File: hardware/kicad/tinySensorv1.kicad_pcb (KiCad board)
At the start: 2 copper layers, 94 x 60 mm, 32 parts, among them J1 RADIO, J10 CR2032 socket, J11 AAA socket, J12 AA Socket, J13 RAW IN, J2 DCDC converter, J3 BMP/BME breakout, J4 PWM out, J5 OneWire sensor, J6 ISP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

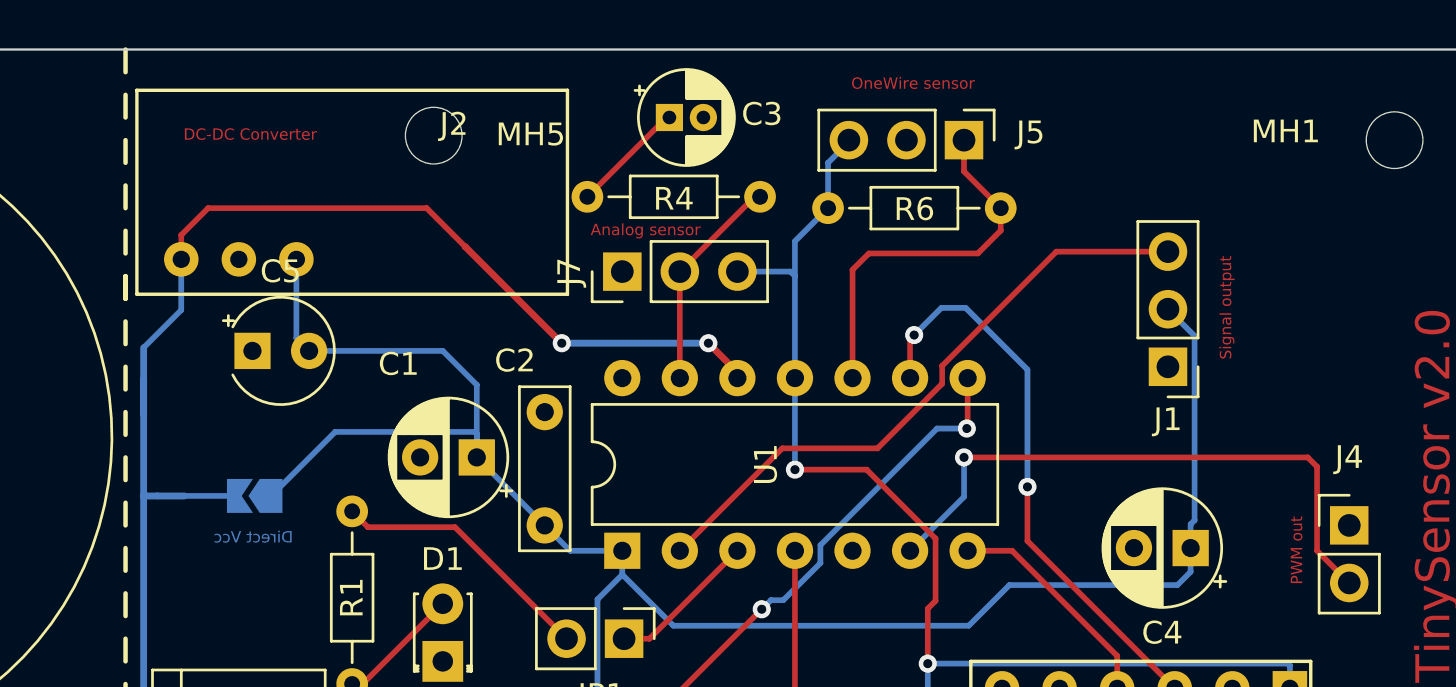
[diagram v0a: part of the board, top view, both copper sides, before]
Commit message: feat: Last enhancements from hardware testing
* Full LM35 support: <0 temp with diode support
* 433Mhz emitter is powered by SENSOR_VCC
* Enhanced layout
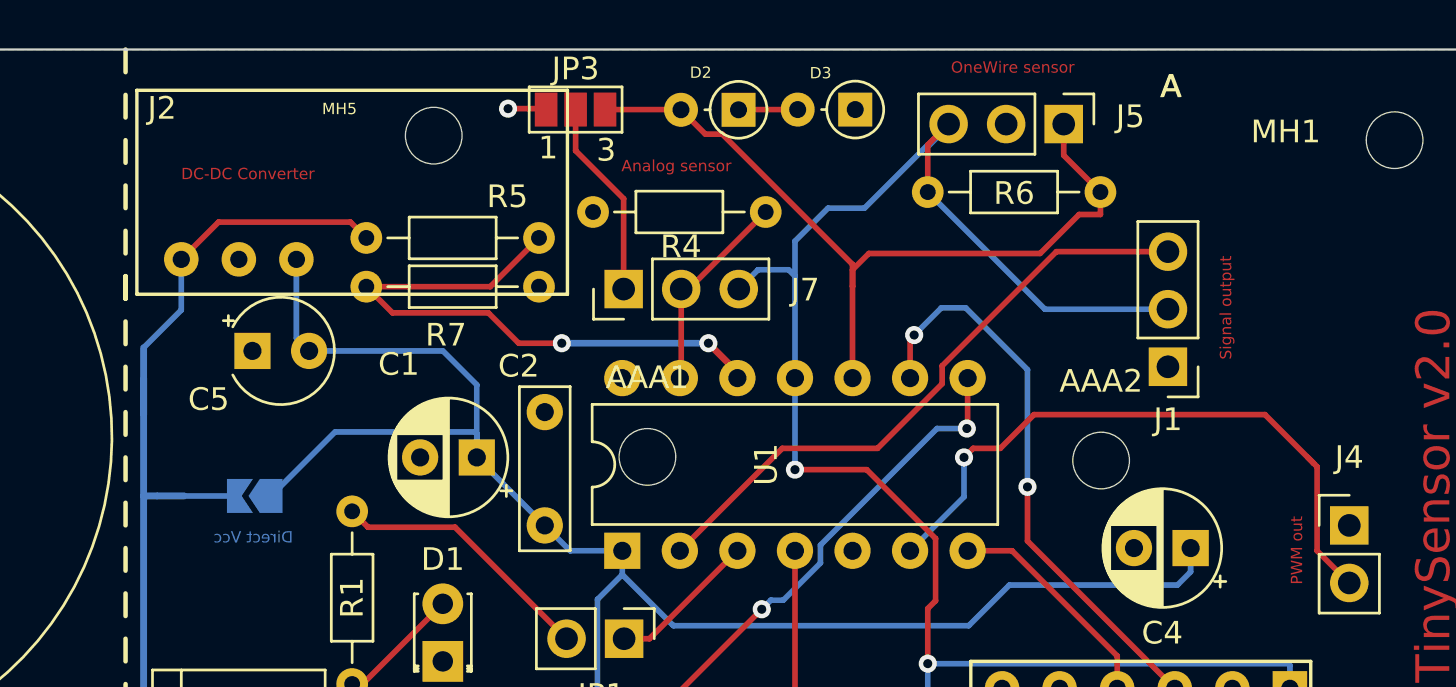
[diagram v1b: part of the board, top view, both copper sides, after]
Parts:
- removed C3: 1u, Capacitor_THT:CP_Radial_D4.0mm_P1.50mm
- added AAA1: MountingHole, MountingHole:MountingHole_2.5mm, F.Cu at (170.0, 66.0)
- added AAA2: MountingHole, MountingHole:MountingHole_2.5mm, F.Cu at (190.1, 66.1)
- added D2: 1N4001, Diode_THT:D_DO-34_SOD68_P2.54mm_Vertical_AnodeUp, F.Cu at (174.1, 50.7)
- added D3: 1N4001, Diode_THT:D_DO-34_SOD68_P2.54mm_Vertical_AnodeUp, F.Cu at (179.2, 50.6)
- added JP3: Ground ref, Jumper:SolderJumper-3_P1.3mm_Open_Pad1.0x1.5mm_NumberLabels, F.Cu at (166.9, 50.6)
- added R5: 1k, Resistor_THT:R_Axial_DIN0204_L3.6mm_D1.6mm_P7.62mm_Horizontal, F.Cu at (165.2, 56.3)
- added R7: 1k, Resistor_THT:R_Axial_DIN0204_L3.6mm_D1.6mm_P7.62mm_Horizontal, F.Cu at (165.2, 58.5)
- R4: value 75R -> 18k
- moved J5 4.46 mm to (188.4, 51.3)
- moved R6 4.46 mm to (182.4, 54.3)
- moved J7 0.77 mm to (169.0, 58.6)
- moved R4 0.72 mm to (175.2, 55.2)
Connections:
- net /OneWire renamed /OneWire_and_analog_bias
- J1 pad 2: VCC -> /SENSOR_VCC
- J7 pad 1: GND -> Net-(J7-Pad1)
- R4 pad 2: Net-(C3-Pad1) -> GND
- U1 pad 12: +BATT -> /Battery_Checker
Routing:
- net /Battery_Checker: track 0.00 -> 26.7 mm, vias 0 -> 2
- net /SENSOR_VCC: track 53.0 -> 74.3 mm
- net +BATT: track 127.8 -> 107.6 mm, vias 2 -> 0
- net /OneWire_and_analog_bias: track 16.7 -> 36.1 mm
- net VCC: track 85.0 -> 73.9 mm
- net Net-(J7-Pad1): track 0.00 -> 8.80 mm
- net Net-(C3-Pad1): track 5.07 -> 0.00 mm
- net Net-(D2-Pad1): track 0.00 -> 2.61 mm
- net /PWM_OUT: track 26.6 -> 28.5 mm
- net GND: track 0.03 -> 1.72 mm, vias 0 -> 1
- net /Analog_sensor: track 9.61 -> 9.09 mm

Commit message: layout enhancements
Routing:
- net /TX_RADIO: track 27.5 -> 29.8 mm
- net /OneWire_and_analog_bias: track 36.1 -> 37.7 mm
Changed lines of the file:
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@@
     (thickness 1.6)
     (drawings 94)
-    (tracks 179)
+    (tracks 180)
     (zones 0)
     (modules 38)
@@
     (solder_mask_min_width 0.25)
     (aux_axis_origin 0 0)
+    (grid_origin 172.92 51.7)
     (visible_elements 7FFDFFFF)
     (pcbplotparams
@@
     (add_net VCC)
   )
+  (module Jumper:SolderJumper-3_P1.3mm_Open_Pad1.0x1.5mm_NumberLabels (layer F.Cu)
+    (at 166.86 50.65)
+    (descr "SMD Solder Jumper, 1x1.5mm Pads, 0.3mm gap, open, labeled with numbers")
+    (tags "solder jumper open")
+    (attr virtual)
+    (fp_text reference JP3 (at 0 -1.8) (layer F.SilkS)
+      (effects (font (size 1 1) (thickness 0.15)))
+    )
+    (fp_text value "Ground ref" (at 0 1.9) (layer F.Fab)
+      (effects (font (size 1 1) (thickness 0.15)))
+    )
+    (fp_line (start 2.3 1.25) (end -2.3 1.25) (layer F.CrtYd) (width 0.05))
+    (fp_line (start 2.3 1.25) (end 2.3 -1.25) (layer F.CrtYd) (width 0.05))
+    (fp_line (start -2.3 -1.25) (end -2.3 1.25) (layer F.CrtYd) (width 0.05))
+    (fp_line (start -2.3 -1.25) (end 2.3 -1.25) (layer F.CrtYd) (width 0.05))
+    (fp_line (start -2.05 -1) (end 2.05 -1) (layer F.SilkS) (width 0.12))
+    (fp_line (start 2.05 -1) (end 2.05 1) (layer F.SilkS) (width 0.12))
+    (fp_line (start 2.05 1) (end -2.05 1) (layer F.SilkS) (width 0.12))
+    (fp_line (start -2.05 1) (end -2.05 -1) (layer F.SilkS) (width 0.12))
+    (fp_text user 1 (at -2.6 0) (layer F.SilkS)
+      (effects (font (size 1 1) (thickness 0.15)))
+    )
+    (fp_text user 3 (at 2.6 0) (layer F.SilkS)
+      (effects (font (size 1 1) (thickness 0.15)))
+    )
+    (pad 1 smd rect (at -1.3 0) (size 1 1.5) (layers F.Cu F.Mask)
+      (net 6 GND))
+    (pad 2 smd rect (at 0 0) (size 1 1.5) (layers F.Cu F.Mask)
+      (net 18 "Net-(J7-Pad1)"))
+    (pad 3 smd rect (at 1.3 0) (size 1 1.5) (layers F.Cu F.Mask)
+      (net 20 /OneWire_and_analog_bias))
+  )
   (module MountingHole:MountingHole_2.5mm locked (layer F.Cu)
     (at 190.05 66.136918)
@@
       (effects (font (size 1 1) (thickness 0.15)))
     )
-    (fp_text user %R (at 1.27 -2.25566 180) (layer F.Fab)
+    (fp_text user %R (at 1.25 -1.92 180) (layer F.Fab)
       (effects (font (size 1 1) (thickness 0.15)))
     )
@@
       (rotate (xyz 0 0 0))
     )
-  )
-  (module Jumper:SolderJumper-3_P1.3mm_Open_Pad1.0x1.5mm_NumberLabels (layer F.Cu)
-    (at 166.86 50.65)
-    (descr "SMD Solder Jumper, 1x1.5mm Pads, 0.3mm gap, open, labeled with numbers")
-    (tags "solder jumper open")
-    (attr virtual)
-    (fp_text reference JP3 (at 0 -1.8) (layer F.SilkS)
-      (effects (font (size 1 1) (thickness 0.15)))
-    )
-    (fp_text value "Ground ref" (at 0 1.9) (layer F.Fab)
-      (effects (font (size 1 1) (thickness 0.15)))
-    )
-    (fp_text user 3 (at 1.35 1.79) (layer F.SilkS)
-      (effects (font (size 1 1) (thickness 0.15)))
-    )
-    (fp_text user 1 (at -1.21 1.69) (layer F.SilkS)
-      (effects (font (size 1 1) (thickness 0.15)))
-    )
-    (fp_line (start -2.05 1) (end -2.05 -1) (layer F.SilkS) (width 0.12))
-    (fp_line (start 2.05 1) (end -2.05 1) (layer F.SilkS) (width 0.12))
-    (fp_line (start 2.05 -1) (end 2.05 1) (layer F.SilkS) (width 0.12))
-    (fp_line (start -2.05 -1) (end 2.05 -1) (layer F.SilkS) (width 0.12))
-    (fp_line (start -2.3 -1.25) (end 2.3 -1.25) (layer F.CrtYd) (width 0.05))
-    (fp_line (start -2.3 -1.25) (end -2.3 1.25) (layer F.CrtYd) (width 0.05))
-    (fp_line (start 2.3 1.25) (end 2.3 -1.25) (layer F.CrtYd) (width 0.05))
-    (fp_line (start 2.3 1.25) (end -2.3 1.25) (layer F.CrtYd) (width 0.05))
-    (pad 3 smd rect (at 1.3 0) (size 1 1.5) (layers F.Cu F.Mask)
-      (net 20 /OneWire_and_analog_bias))
-    (pad 2 smd rect (at 0 0) (size 1 1.5) (layers F.Cu F.Mask)
-      (net 18 "Net-(J7-Pad1)"))
-    (pad 1 smd rect (at -1.3 0) (size 1 1.5) (layers F.Cu F.Mask)
-      (net 6 GND))
   )
   (module Resistor_THT:R_Axial_DIN0204_L3.6mm_D1.6mm_P7.62mm_Horizontal (layer F.Cu)
@@
     (effects (font (size 0.5 0.5) (thickness 0.125)) (justify mirror))
   )
-  (gr_text "OneWire sensor" (at 186.15 48.79) (layer F.Cu)
+  (gr_text "OneWire sensor" (at 185.77 49.2) (layer F.Cu)
     (effects (font (size 0.5 0.5) (thickness 0.125)))
   )
-  (gr_text "Analog sensor" (at 171.31 53.14) (layer F.Cu)
+  (gr_text "Analog sensor" (at 171.72 53.72) (layer F.Cu)
     (effects (font (size 0.5 0.5) (thickness 0.125)))
   )
@@
   (segment (start 170.12 74) (end 169 74) (width 0.25) (layer F.Cu) (net 2) (status 20))
   (segment (start 174 70.12) (end 170.12 74) (width 0.25) (layer F.Cu) (net 2) (status 10))
-  (segment (start 171.46 70.12) (end 175.98 65.6) (width 0.25) (layer F.Cu) (net 4) (status 10))
-  (segment (start 180.185002 65.6) (end 175.98 65.6) (width 0.25) (layer F.Cu) (net 4))
-  (segment (start 183.034999 62.750003) (end 180.185002 65.6) (width 0.25) (layer F.Cu) (net 4))
-  (segment (start 183.034999 61.959999) (end 183.034999 62.750003) (width 0.25) (layer F.Cu) (net 4))
-  (segment (start 188.074998 56.92) (end 183.034999 61.959999) (width 0.25) (layer F.Cu) (net 4))
-  (segment (start 193 56.92) (end 188.074998 56.92) (width 0.25) (layer F.Cu) (net 4) (status 10))
+  (segment (start 189.26 60.66) (end 193 56.92) (width 0.25) (layer F.Cu) (net 4))
+  (segment (start 182.96 60.66) (end 189.26 60.66) (width 0.25) (layer F.Cu) (net 4))
+  (segment (start 182.96 65.46) (end 182.96 60.66) (width 0.25) (layer F.Cu) (net 4))
+  (segment (start 182.82 65.6) (end 182.96 65.46) (width 0.25) (layer F.Cu) (net 4))
+  (segment (start 171.46 70.12) (end 175.98 65.6) (width 0.25) (layer F.Cu) (net 4))
+  (segment (start 175.98 65.6) (end 182.82 65.6) (width 0.25) (layer F.Cu) (net 4))
   (segment (start 190.76 76.66) (end 190.76 76.19) (width 0.25) (layer F.Cu) (net 5) (status 30))
   (segment (start 184.16 70.12) (end 186.12 70.12) (width 0.25) (layer F.Cu) (net 5) (status 10))
@@
   (segment (start 188.4 52.67) (end 190.02 54.29) (width 0.25) (layer F.Cu) (net 20) (status 20))
   (segment (start 188.4 51.29) (end 188.4 52.67) (width 0.25) (layer F.Cu) (net 20) (status 10))
-  (segment (start 179.8 57) (end 179.08 57.72) (width 0.25) (layer F.Cu) (net 20))
-  (segment (start 187.358588 57) (end 179.8 57) (width 0.25) (layer F.Cu) (net 20))
   (segment (start 189.078639 55.279949) (end 187.358588 57) (width 0.25) (layer F.Cu) (net 20))
   (segment (start 190.02 55.279949) (end 189.078639 55.279949) (width 0.25) (layer F.Cu) (net 20))
@@
   (segment (start 171.5 50.65) (end 171.51 50.66) (width 0.25) (layer F.Cu) (net 20))
   (segment (start 168.16 50.65) (end 171.5 50.65) (width 0.25) (layer F.Cu) (net 20))
-  (segment (start 179.08 57.482998) (end 179.08 58.46) (width 0.25) (layer F.Cu) (net 20))
-  (segment (start 173.332003 51.735001) (end 179.08 57.482998) (width 0.25) (layer F.Cu) (net 20))
-  (segment (start 172.585001 51.735001) (end 173.332003 51.735001) (width 0.25) (layer F.Cu) (net 20))
-  (segment (start 171.51 50.66) (end 172.585001 51.735001) (width 0.25) (layer F.Cu) (net 20))
-  (segment (start 179.08 57.72) (end 179.08 58.46) (width 0.25) (layer F.Cu) (net 20))
   (segment (start 179.08 58.46) (end 179.08 62.5) (width 0.25) (layer F.Cu) (net 20))
+  (segment (start 171.51 51.72066) (end 172.70934 52.92) (width 0.25) (layer F.Cu) (net 20))
+  (segment (start 171.51 50.66) (end 171.51 51.72066) (width 0.25) (layer F.Cu) (net 20))
+  (segment (start 172.70934 52.92) (end 178.11 52.92) (width 0.25) (layer F.Cu) (net 20))
+  (segment (start 187.358588 57) (end 179.98 57) (width 0.25) (layer F.Cu) (net 20))
+  (segment (start 179.98 57.56) (end 179.08 58.46) (width 0.25) (layer F.Cu) (net 20))
+  (segment (start 179.98 57) (end 179.98 57.56) (width 0.25) (layer F.Cu) (net 20))
+  (segment (start 179.98 54.79) (end 178.11 52.92) (width 0.25) (layer F.Cu) (net 20))
+  (segment (start 179.98 57) (end 179.98 54.79) (width 0.25) (layer F.Cu) (net 20))
   (zone (net 6) (net_name GND) (layer B.Cu) (hatch edge 0.508)
     (connect_pads (clearance 0.508))

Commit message: feat: Allow shutdown of DCDC stepup
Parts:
- added JP4: Power ctrl, Jumper:SolderJumper-3_P1.3mm_Open_Pad1.0x1.5mm_NumberLabels, F.Cu at (158.9, 50.4)
- added Q1: BS170, Package_TO_SOT_THT:TO-92_Inline, F.Cu at (150.3, 51.9)
- J2: value DCDC converter -> DC-DC step up; footprint TinySensor lib:DC-DC_0.9v-3.3v_to_3.3v -> Connector_PinHeader_2.54mm:PinHeader_1x03_P2.54mm_Vertical
- moved MH5 19.4 mm to (141.2, 51.7)
- moved J2 3.26 mm to (150.1, 56.8), turned to 90 degrees
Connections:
- C1 pad 2: GND -> Net-(C1-Pad2)
- C2 pad 1: GND -> Net-(C1-Pad2)
- C5 pad 1: GND -> Net-(C1-Pad2)
- J2 pad 2: GND -> Net-(C1-Pad2)
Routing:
- net /PWM_OUT: track 28.5 -> 82.0 mm
- net Net-(C1-Pad2): track 0.00 -> 32.0 mm, vias 0 -> 1
- net Net-(JP4-Pad1): track 0.00 -> 8.28 mm
- net +BATT: track 107.6 -> 112.5 mm
- net GND: track 1.72 -> 5.43 mm
- net VCC: track 73.9 -> 71.9 mm
